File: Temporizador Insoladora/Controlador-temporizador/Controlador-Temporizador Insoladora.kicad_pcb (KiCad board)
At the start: 2 copper layers, 113 x 66 mm, 75 parts, among them P1 ICSP, P2 VAC12V, P3 CARGA, P4 TRANSF, P5 VAC, P6 OPTO, P7 CONN_02X08, P8 OPTO, Q1 BC548, Q2 BC548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

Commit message: Acomodando el controlador
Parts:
- moved C3 9.25 mm to (86.4, 81.3)
- moved C9 7.45 mm to (94.0, 81.4)
- moved R16 5.08 mm to (102.9, 82.5)
- moved U1 4.58 mm to (80.0, 81.3)
- moved D1 3.81 mm to (90.2, 101.6)
- moved P1 3.81 mm to (86.4, 101.6)
- moved R1 3.59 mm to (92.7, 102.9)
- moved R20 2.54 mm to (108.0, 82.5)
- moved R17 2.54 mm to (105.4, 82.5)
- moved C4 1.27 mm to (85.1, 110.5)
- moved D4 1.27 mm to (95.2, 101.6)
- moved SW1 1.27 mm to (91.4, 111.8)
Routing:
- net Net-(C4-Pad1): track 23.4 -> 0.01 mm
- net VCC: track 136.2 -> 131.4 mm
- net PGC: track 21.4 -> 17.6 mm
- net PGD: track 17.0 -> 13.2 mm
- net SUBIR: track 15.5 -> 13.0 mm
- net ~MCLR~/VPP: track 29.3 -> 27.5 mm
- net BAJAR: track 13.0 -> 12.0 mm
- net Net-(C8-Pad1): track 22.6 -> 23.2 mm
- added copper zone on B.Cu, net Net-(C4-Pad1)

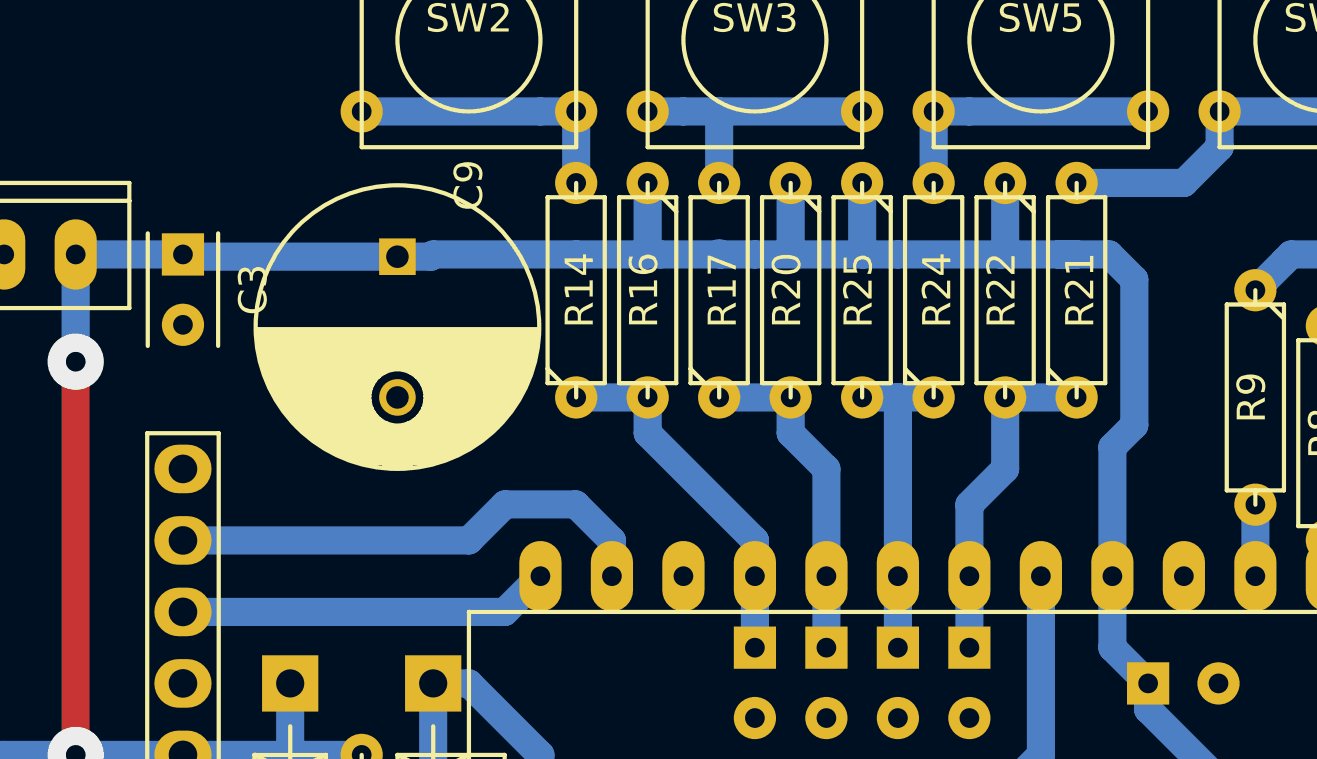
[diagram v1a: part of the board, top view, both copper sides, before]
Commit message: Acomodando ruteo y componentes de pcb controlador
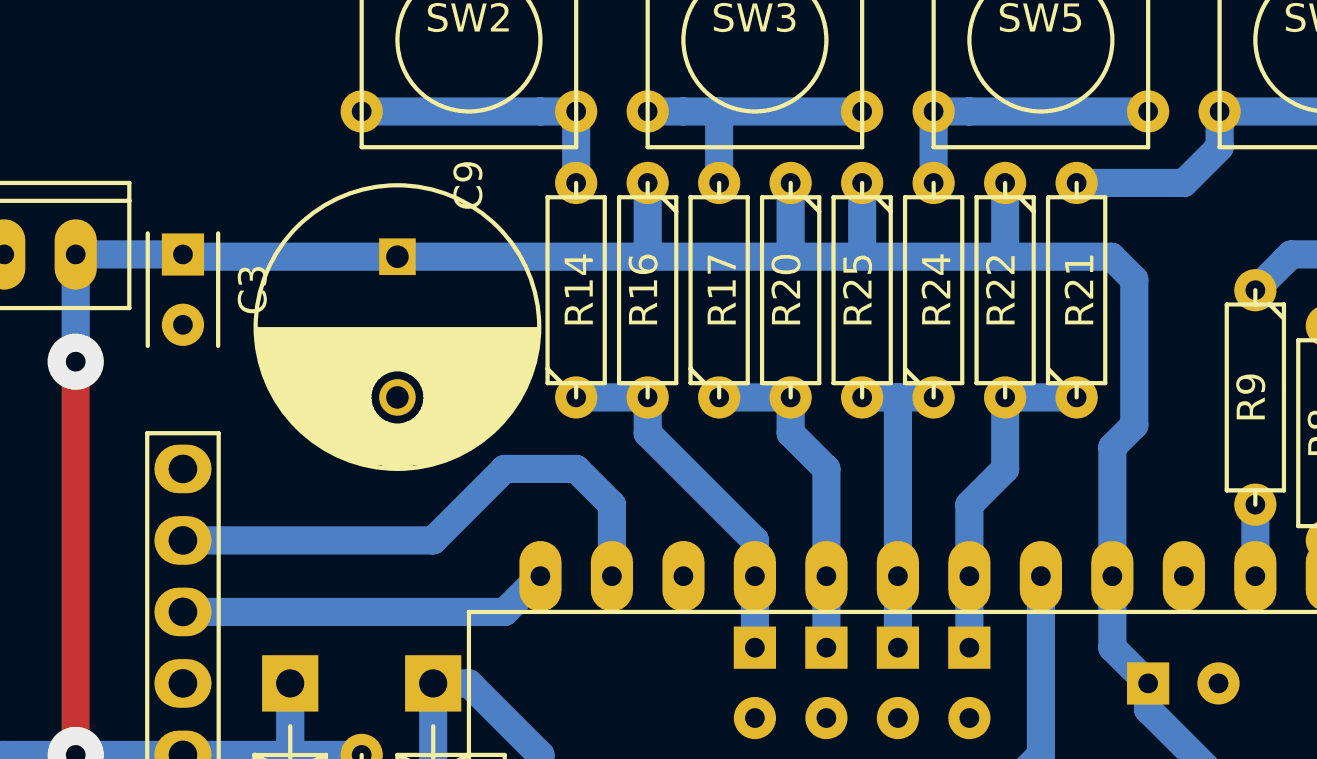
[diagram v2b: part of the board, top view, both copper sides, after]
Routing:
- net PGC: track 17.6 -> 19.4 mm
- net VCC: track 131.4 -> 130.8 mm

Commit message: Sigo acomodando controlador
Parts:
- moved R12 11.4 mm to (82.5, 113.0)
- moved C4 4.58 mm to (87.6, 106.7), turned to 180 degrees
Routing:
- net VCC: track 130.8 -> 142.2 mm
- net CPZ: track 62.8 -> 55.5 mm

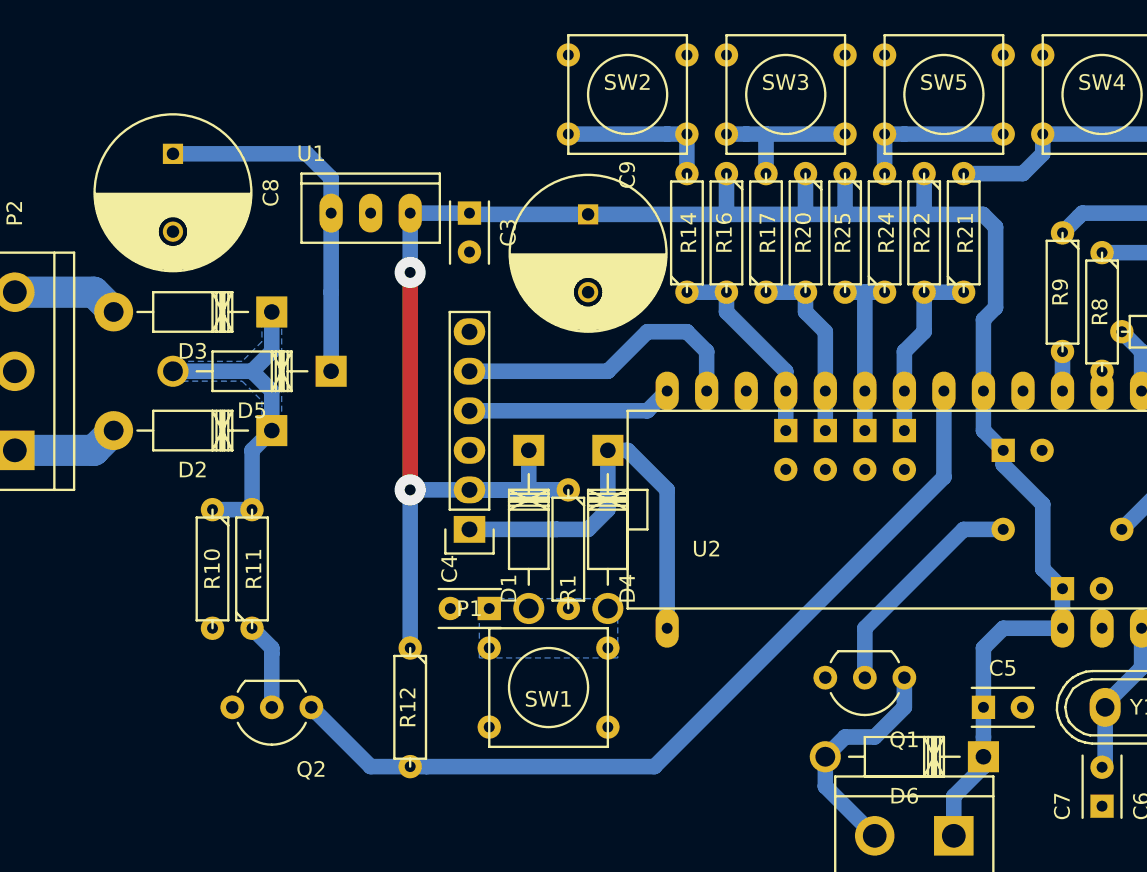
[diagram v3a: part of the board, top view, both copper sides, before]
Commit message: Quitado pulsador de reset por ser irrelevante para la aplicación
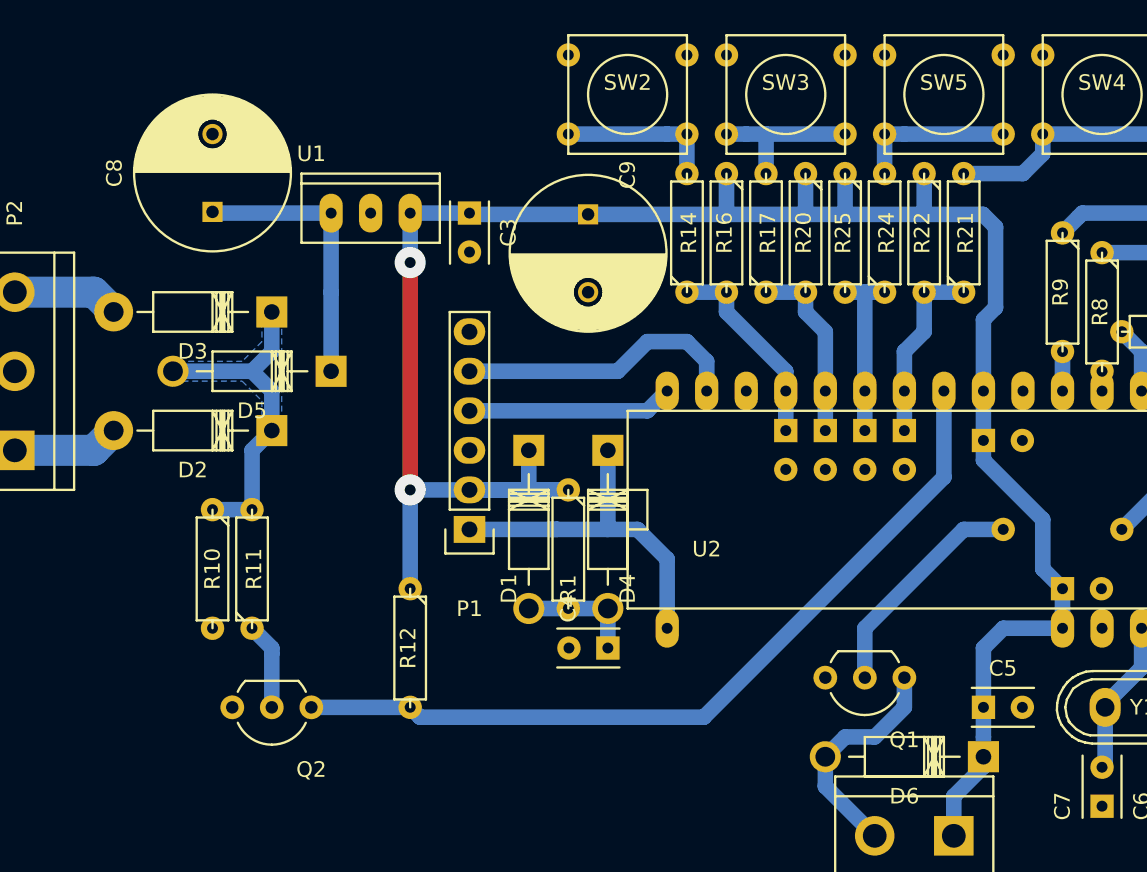
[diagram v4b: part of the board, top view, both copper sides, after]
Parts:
- removed SW1: Reset, Buttons_Switches_ThroughHole:SW_PUSH_SMALL
- moved C4 8.03 mm to (95.2, 109.2)
- moved C8 4.51 mm to (69.8, 81.2), turned to 90 degrees
- moved R12 3.81 mm to (82.5, 109.2)
- moved C1 1.42 mm to (119.4, 95.9)
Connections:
- P1 pad 6: Net-(P1-Pad6) -> (no net)
- P5 pad 2: Earth -> (no net)
- U2 pad 24: Net-(U2-Pad24) -> (no net)
- U2 pad 25: Net-(U2-Pad25) -> (no net)
- U2 pad 26: Net-(U2-Pad26) -> (no net)
- U2 pad 38: Net-(U2-Pad38) -> (no net)
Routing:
- net Net-(C4-Pad1): track 0.00 -> 7.62 mm
- net Net-(C8-Pad1): track 23.2 -> 17.8 mm
- net ~MCLR~/VPP: track 27.5 -> 23.6 mm
- net VCC: track 142.2 -> 138.4 mm
- net CPZ: track 55.5 -> 52.8 mm
- net PGC: track 19.4 -> 18.5 mm
- removed copper zone on B.Cu, net Net-(C4-Pad1)

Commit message: Reacomodando controlador
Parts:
- C1, C2: moved to F.Cu
- R12: moved to B.Cu
- moved R12 39.8 mm to (120.7, 97.8), turned to 180 degrees
- moved D1 6.35 mm to (90.2, 108.0)
- moved P6 5.75 mm to (120.7, 121.9)
- moved C1 5.72 mm to (119.4, 90.2)
- moved C2 5.24 mm to (123.2, 110.5), turned to 180 degrees
- moved C9 5.00 mm to (94.0, 86.4), turned to 90 degrees
- moved Q1 3.86 mm to (118.1, 110.5)
- moved C4 3.81 mm to (95.2, 113.0)
- moved D4 3.81 mm to (95.2, 105.4)
- moved D6 3.81 mm to (118.1, 116.2)
- moved P1 3.81 mm to (86.4, 105.4)
- moved R1 3.81 mm to (92.7, 106.7)
- moved C5 3.77 mm to (123.2, 113.0), turned to 180 degrees
- moved C6 1.27 mm to (133.3, 119.3)
- moved C7 1.27 mm to (128.3, 119.4)
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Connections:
- net Net-(C6-Pad2) renamed /Xtal-
- net Net-(C7-Pad2) renamed /Xtal+
- P1 pad 6: (no net) -> Net-(P1-Pad6)
- P5 pad 2: (no net) -> Earth
- U2 pad 24: (no net) -> Net-(U2-Pad24)
- U2 pad 25: (no net) -> Net-(U2-Pad25)
- U2 pad 26: (no net) -> Net-(U2-Pad26)
- U2 pad 38: (no net) -> Net-(U2-Pad38)
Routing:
- net VCC: track 138.4 -> 127.2 mm
- net CPZ: track 52.8 -> 61.2 mm
- net ~MCLR~/VPP: track 23.6 -> 20.1 mm
- net Net-(D6-Pad1): track 14.7 -> 17.8 mm
- net Net-(C4-Pad1): track 7.62 -> 9.42 mm
- net PGC: track 18.5 -> 20.0 mm
- net PGD: track 13.2 -> 14.8 mm
- net SALIDAOPTO: track 19.1 -> 17.9 mm
- net Net-(Q1-Pad2): track 14.7 -> 13.7 mm
- net /Xtal+: track 10.0 -> 9.46 mm

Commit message: Acomodando controlador
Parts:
- removed D6: 1N4007, Diodes_ThroughHole:Diode_DO-41_SOD81_Horizontal_RM10
- added P9: OPTO, Connect:bornier2, F.Cu at (110.5, 121.9)
- added Q7: BC548, Housings_TO-92:TO-92_Inline_Wide, F.Cu at (106.7, 110.5)
- added R30: 1K, Discret:R3, B.Cu at (125.7, 101.6)
- moved R10 32.5 mm to (97.8, 120.7), turned to 0 degrees
- moved R11 29.0 mm to (97.8, 118.1), turned to 180 degrees
- moved Q2 28.0 mm to (104.1, 114.3)
- moved C5 2.80 mm to (122.0, 115.6), turned to 0 degrees
- moved R13 2.54 mm to (125.7, 104.1)
- moved C2 1.77 mm to (122.0, 111.8), turned to 0 degrees
- moved R12 1.27 mm to (120.7, 99.1)
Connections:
- net SALIDAOPTO renamed SALIDAOPTO0
- U2 pad 24: Net-(U2-Pad24) -> SALIDAOPTO1
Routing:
- net CPZ: track 61.2 -> 28.3 mm
- net Net-(D2-Pad2): track 21.9 -> 53.5 mm
- net Net-(Q7-Pad2): track 0.00 -> 17.1 mm
- net SALIDAOPTO1: track 0.00 -> 16.8 mm
- net VCC: track 127.2 -> 140.3 mm
- net Net-(P9-Pad2): track 0.00 -> 12.0 mm
- net Net-(P6-Pad2): track 17.8 -> 13.3 mm
- net SALIDAOPTO0: track 17.9 -> 21.2 mm
- net Net-(Q1-Pad2): track 13.7 -> 10.5 mm
- net Net-(Q2-Pad2): track 5.61 -> 3.81 mm

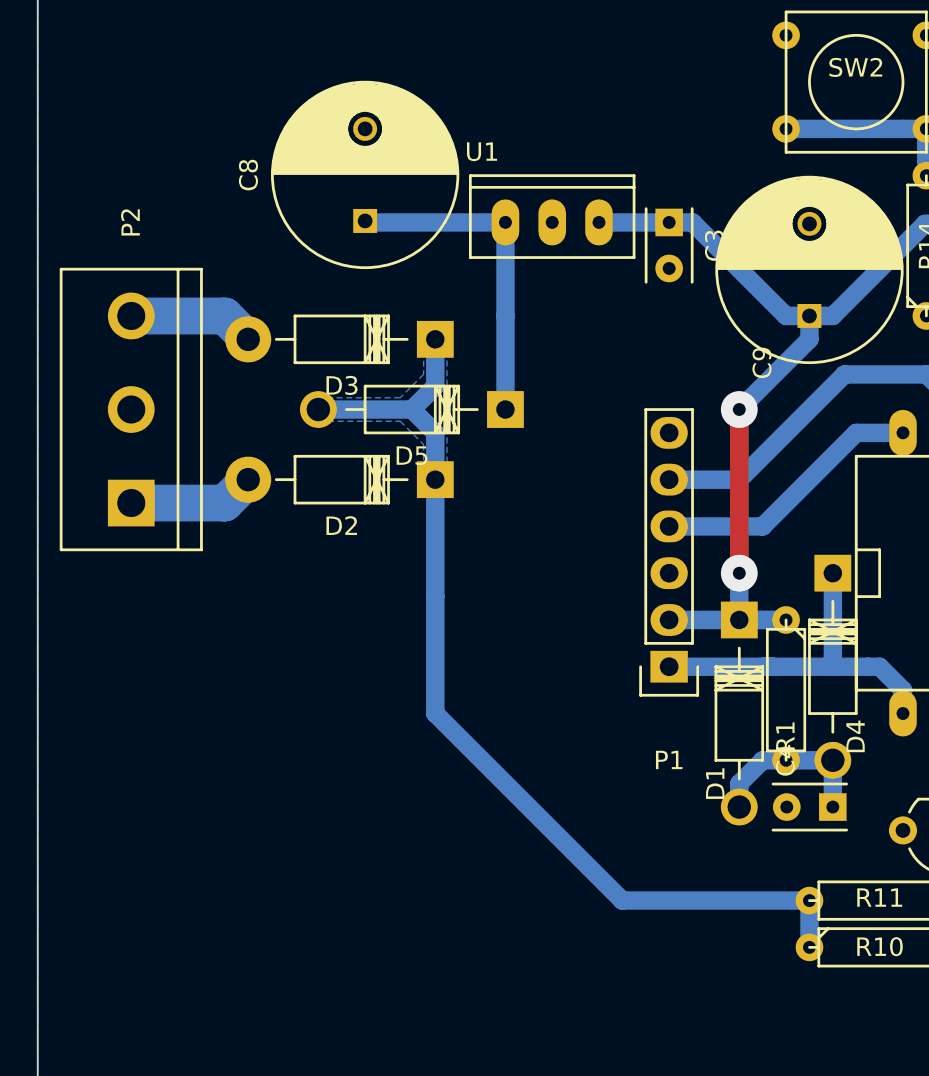
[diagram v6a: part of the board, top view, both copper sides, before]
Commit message: Cambio del lugar donde se detecta el cruce por cero
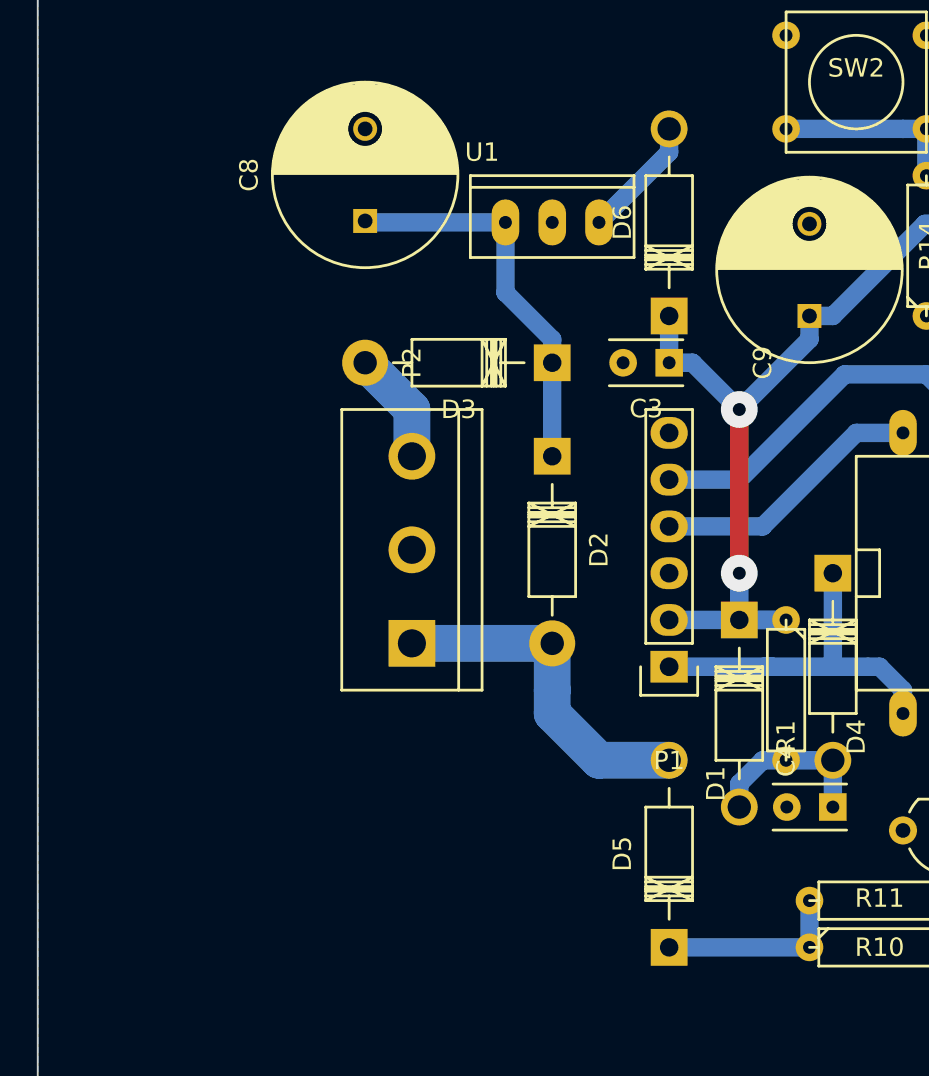
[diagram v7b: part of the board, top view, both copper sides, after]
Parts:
- added D6: 1N4007, Diodes_ThroughHole:Diode_DO-41_SOD81_Horizontal_RM10, F.Cu at (86.4, 81.3)
- moved D5 27.9 mm to (86.4, 115.6), turned to 270 degrees
- moved P2 17.0 mm to (72.4, 99.1)
- moved D2 12.0 mm to (80.0, 99.1), turned to 90 degrees
- moved C3 7.62 mm to (86.4, 88.9), turned to 180 degrees
- moved D3 6.48 mm to (74.9, 88.9)
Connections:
- D2 pad 2: Net-(D2-Pad2) -> Net-(C8-Pad1)
- D3 pad 2: Net-(D2-Pad2) -> Net-(C8-Pad1)
- D5 pad 1: Net-(D2-Pad2) -> Net-(D2-Pad1)
- D5 pad 2: Net-(C8-Pad1) -> Net-(D5-Pad2)
- R10 pad 1: Net-(D2-Pad2) -> Net-(D5-Pad2)
- R11 pad 2: Net-(D2-Pad2) -> Net-(D5-Pad2)
- U1 pad VO: VCC -> Net-(D6-Pad1)
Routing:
- net Net-(D2-Pad2): track 53.5 -> 0.00 mm
- net Net-(D2-Pad1): track 6.88 -> 18.8 mm
- net Net-(D5-Pad2): track 0.00 -> 10.2 mm
- net Net-(D6-Pad1): track 0.00 -> 6.66 mm
- net VCC: track 140.3 -> 134.1 mm
- net Net-(C8-Pad1): track 17.8 -> 21.4 mm
- net Net-(D3-Pad1): track 6.88 -> 6.13 mm
- removed copper zone on B.Cu, net Net-(D2-Pad2)
